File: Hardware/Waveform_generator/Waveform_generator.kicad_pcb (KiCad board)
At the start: 2 copper layers, 83.8 x 100 mm, 92 parts, among them J1 Conn_01x02, J2 Conn_01x02, J3 Conn_01x02, J4 Conn_01x02, SW1 SW_DPDT_x2, U1 TPS54202DDC, U10 MCP4822, U11 LM1875, U2 TL072, U3 ESP32-DEVKITC-32U, U4 TSR1-2450E, U5 XC6206PxxxMR, U6 AD9837BCPZ-RL7, U7 TL072, U8 AD5160, U9 TL072, Y1 X1G0041710027

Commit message: Revisión 1 del hardware. Reorganizaco un poco el layout y añadidos shottky de protección, puente para desconectar el buck, conectores de pogo para conectar a masa la carcasa de aluminio, agrandado el espacio del powerOpAmp para un mayor disipador...
Actualizado el controlador para que por USB no printee la batería todo el rato.

Añadida opción de reseteo del AD9837 en cada comando para probar si se soluciona el problema  (no genera nada a la salida)
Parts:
- added D6: SS34, Diode_SMD:D_SMA, F.Cu at (101.5, 129.1)
- added H1: MountingHole_Pad, MountingHole:MountingHole_3.2mm_M3_Pad_TopBottom, F.Cu at (101.7, 87.8)
- added J5: PogoPin, CUSTOM:Pogo pin 1x3 2.54mm male horizontal, F.Cu at (133.3, 49.0)
- added J6: PogoPin, CUSTOM:Pogo pin 1x3 2.54mm male horizontal, F.Cu at (108.6, 133.2)
- added J7: GND_CHASIS, Connector_PinHeader_2.54mm:PinHeader_1x03_P2.54mm_Vertical, F.Cu at (137.6, 59.4)
- added J8: GND_CHASIS, Connector_PinHeader_2.54mm:PinHeader_1x02_P2.54mm_Vertical, F.Cu at (108.6, 126.5)
- added R32: 0R, Resistor_SMD:R_0805_2012Metric_Pad1.20x1.40mm_HandSolder, F.Cu at (137.1, 74.4)
- added TP13: TP, TestPoint:TestPoint_THTPad_D2.0mm_Drill1.0mm, F.Cu at (135.9, 54.9)
- added TP15: Buck out, TestPoint:TestPoint_THTPad_D2.0mm_Drill1.0mm, F.Cu at (124.8, 98.2)
- moved C8 17.6 mm to (83.0, 132.7)
- moved U5 17.3 mm to (80.3, 132.5), turned to -90 degrees
- moved C9 16.8 mm to (77.8, 132.2), turned to -90 degrees
- moved C7 5.60 mm to (90.3, 125.2), turned to -90 degrees
- moved C10 4.41 mm to (85.1, 125.1)
- moved C14 4.36 mm to (82.6, 122.0)
- moved C16 4.15 mm to (81.8, 125.7), turned to 180 degrees
- moved TP6 4.05 mm to (88.8, 118.9)
- moved U6 3.74 mm to (85.0, 120.4)
- moved TP14 3.67 mm to (90.4, 79.1)
- moved Y1 2.69 mm to (88.3, 125.0)
- moved C13 2.40 mm to (82.6, 123.9), turned to 180 degrees
- moved R25 1.51 mm to (78.7, 75.8)
- moved R23 1.50 mm to (81.1, 74.9)
- moved R22 1.50 mm to (76.0, 82.5)
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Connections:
- C1 pad 1: +12V -> /12V_buck
- C2 pad 1: +12V -> /12V_buck
- C5 pad 1: +5V -> /5V_buck
- C6 pad 1: +5V -> /5V_buck
- L1 pad 2: +5V -> /5V_buck
- R7 pad 2: +5V -> /5V_buck
- SW1 pad 1: +12V_IN -> unconnected-(SW1A-A-Pad1)
- SW1 pad 3: unconnected-(SW1A-C-Pad3) -> +12V_IN
- SW1 pad 4: unconnected-(SW1B-A-Pad4) -> -12V_IN
- SW1 pad 6: -12V_IN -> unconnected-(SW1B-C-Pad6)
- U1 pad 3: +12V -> /12V_buck
- U4 pad 3: +5V -> /5V_buck
- Y1 pad 1: unconnected-(Y1-~{ST}-Pad1) -> +3V3
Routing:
- net +5V: track 133.4 -> 31.4 mm
- net /5V_buck: track 0.00 -> 98.9 mm
- net +12V: track 211.4 -> 195.6 mm
- net -12V_IN: track 51.0 -> 36.3 mm
- net /12V_buck: track 0.00 -> 14.0 mm
- net +3V3: track 64.2 -> 52.2 mm, vias 1 -> 0
- net MOSI: track 64.0 -> 58.1 mm
- net LED_Bluetooth: track 28.8 -> 34.0 mm
- net GND: track 14.8 -> 9.61 mm, vias 16 -> 29
- net GNDS: track 0.00 -> 4.83 mm
- net SCK: track 41.0 -> 36.4 mm
- net +3.3VA: track 43.1 -> 47.5 mm, vias 3 -> 2
- net GNDS1: track 0.00 -> 4.08 mm
- net Net-(U6-VOUT): track 2.04 -> 5.74 mm
- net ~{CS_WG}: track 14.7 -> 11.2 mm, vias 1 -> 0
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- added copper zone on B.Cu, net GNDS
- added copper zone on F.Cu, net GNDS
- added copper zone on B.Cu, net GNDS1
- added copper zone on F.Cu, net GNDS1
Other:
- board text added: "+5V"

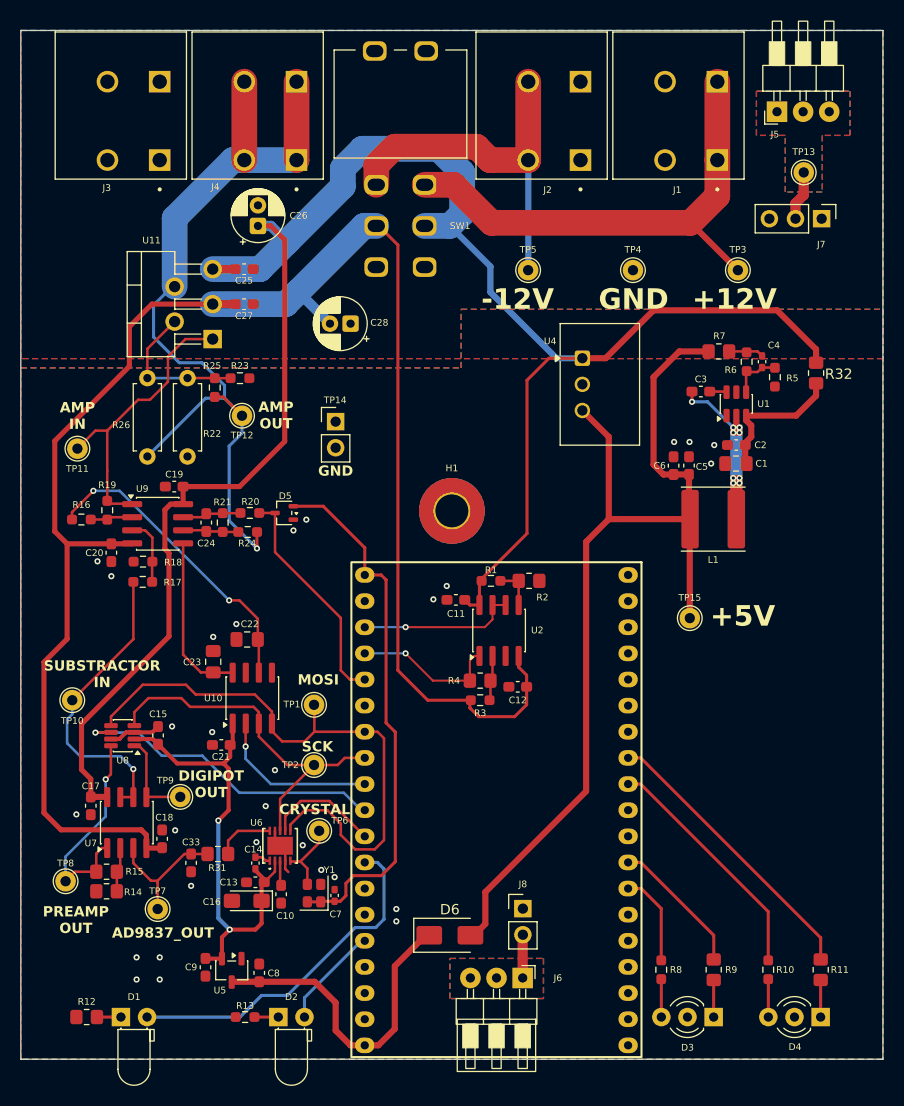
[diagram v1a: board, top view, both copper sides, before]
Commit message: Rev 2 de hardware actualizada con error en los pines del ad9837 (SCLK y CS intercambiados). ERROR IDENTIFICADO
Añadida corrección del offset que hay a la salida del ad9837 que antes no se tenía en cuenta.
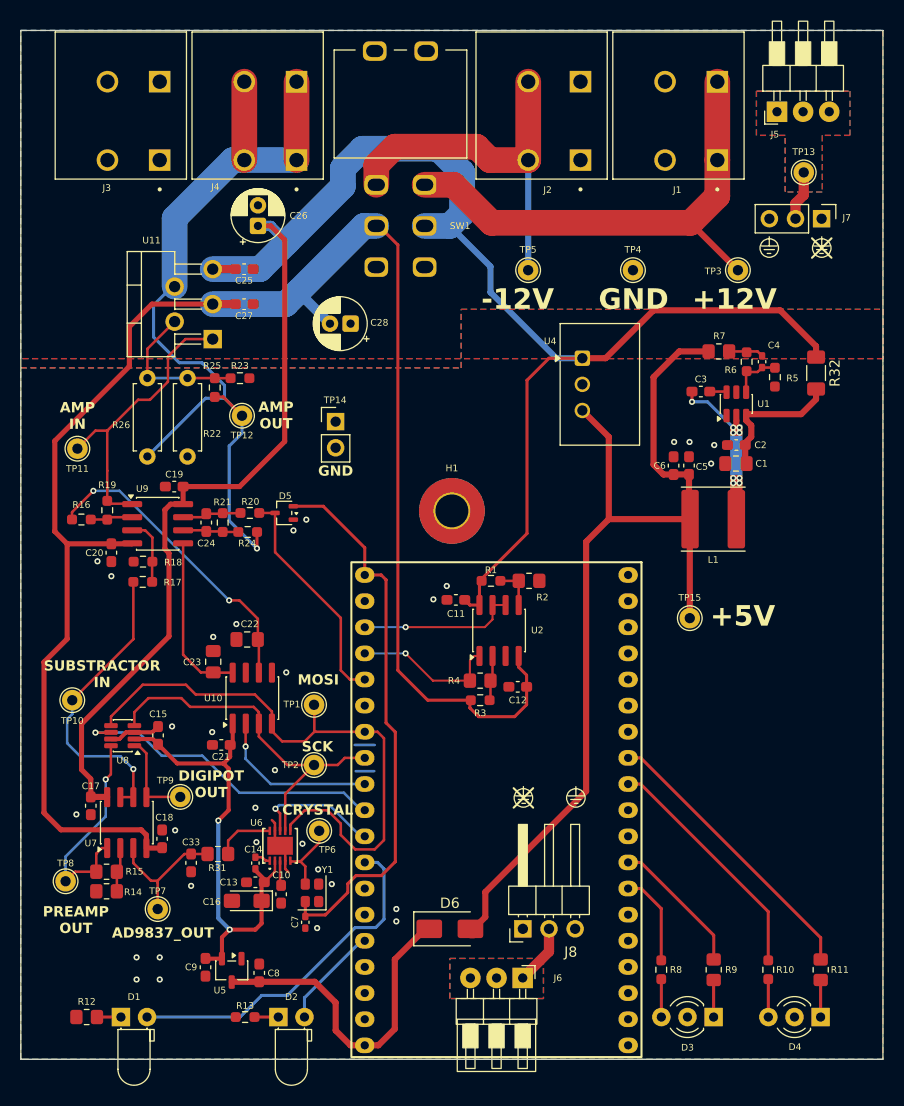
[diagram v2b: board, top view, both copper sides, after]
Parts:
- added G***: LOGO, customfootprints.preety:UCM, B.Cu at (131.5, 107.4)
- added G***: LOGO, customfootprints.preety:GD7mid, B.Cu at (131.7, 121.7)
- J8: footprint Connector_PinHeader_2.54mm:PinHeader_1x02_P2.54mm_Vertical -> Connector_PinHeader_2.54mm:PinHeader_1x03_P2.54mm_Horizontal
- R32: footprint Resistor_SMD:R_0805_2012Metric_Pad1.20x1.40mm_HandSolder -> Resistor_SMD:R_1206_3216Metric_Pad1.30x1.75mm_HandSolder
- moved C7 3.87 mm to (87.5, 127.8), turned to 90 degrees
- moved J8 1.97 mm to (108.6, 128.4), turned to 90 degrees
- moved D6 0.62 mm to (101.5, 128.4)
- moved Y1 0.20 mm to (88.1, 124.9)
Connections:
- J8 pad 1: GND -> unconnected-(J8-Pin_1-Pad1)
- U6 pad 7: ~{CS_WG} -> SCK
- U6 pad 8: SCK -> ~{CS_WG}
- Y1 pad 1: +3V3 -> unconnected-(Y1-~{ST}-Pad1)
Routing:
- net GND: track 9.61 -> 14.5 mm, vias 29 -> 31
- net +3V3: track 52.2 -> 54.2 mm
- net GNDS1: track 4.08 -> 5.84 mm
- net ~{CS_WG}: track 11.2 -> 12.4 mm, vias 0 -> 1
- net +5V: track 31.4 -> 32.0 mm
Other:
- board text added: "Designed by: Guillermo Díaz Rev: 2 Date: 18/08/2026"

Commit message: Añadido switch para el output en el esquemático
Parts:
- added D7: 1N5819WS, Diode_SMD:D_SOD-323_HandSoldering, F.Cu at (106.3, 107.9)
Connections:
- R24 pad 2: /Signal_out -> Net-(Q1-D)
- R25 pad 2: /Signal_out -> Net-(Q1-D)
- R26 pad 2: /Signal_out -> Net-(Q1-D)
- U11 pad 4: /Signal_out -> Net-(Q1-D)
- U3 pad 18: unconnected-(U3-IO23-Pad18) -> Output_EN
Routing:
- net -12V: track 170.9 -> 174.2 mm
- net Net-(D7-K): track 4.38 -> 6.19 mm
